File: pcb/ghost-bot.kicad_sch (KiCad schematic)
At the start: 42 parts, among them J1 Conn_01x03_Pin, J2 Conn_01x03_Pin, J3 Conn_01x04_Pin, J4 Conn_01x02_Pin, J5 Conn_01x05_Pin, J6 Conn_01x04_Pin, SW1 SW_Push, SW2 SW_Push, SW3 Switch

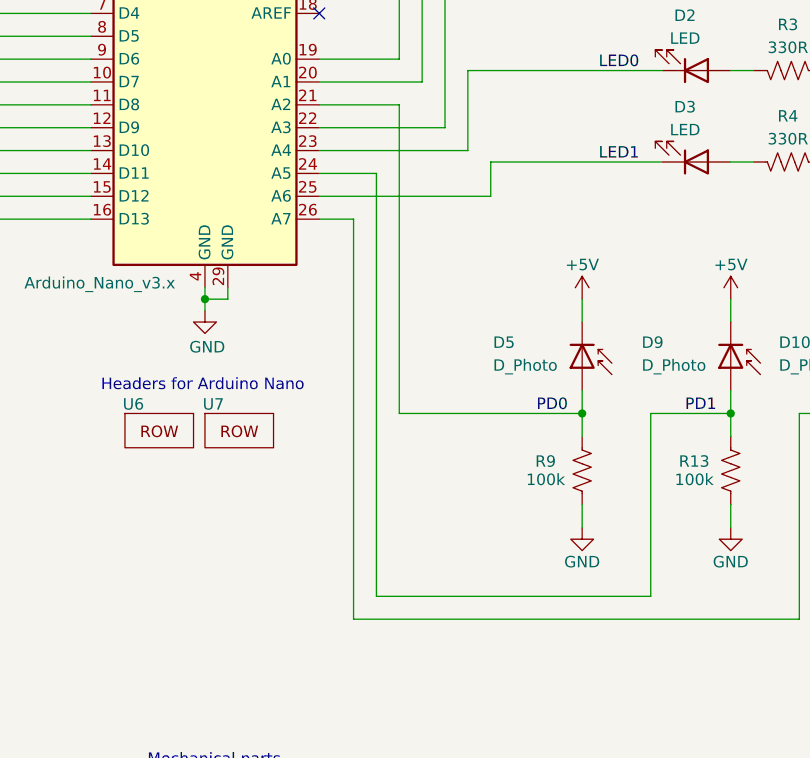
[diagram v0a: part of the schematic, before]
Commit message: Issue: Fix LED1 pin:  Attempted to swap A5 and A6 in schematic and PCB (although not sure what I may of broken in the mean time).
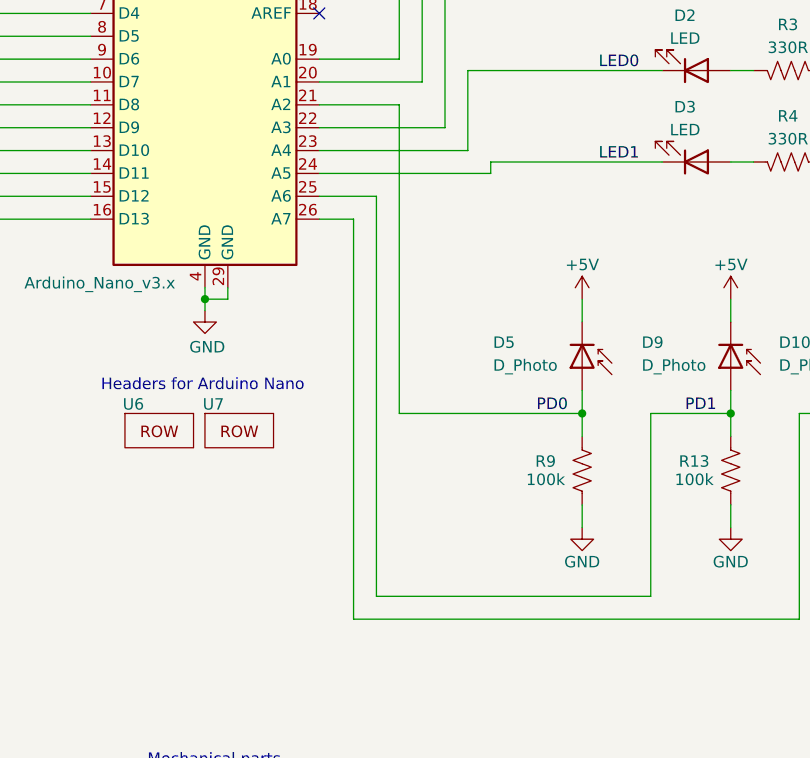
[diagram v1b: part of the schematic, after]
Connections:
- net LED1: now also A1.24 (A5); no longer A1.25 (A6)
- net PD1: now also A1.25 (A6); no longer A1.24 (A5)
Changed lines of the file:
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@@
+	(wire
+		(pts
+			(xy 165.1 99.06) (xy 184.15 99.06)
+		)
+		(stroke
+			(width 0)
+			(type default)
+		)
+	)
 	(wire
 		(pts
@@
 	(wire
 		(pts
+			(xy 165.1 101.6) (xy 171.45 101.6)
+		)
+		(stroke
+			(width 0)
+			(type default)
+		)
+	)
+	(wire
+		(pts
 			(xy 179.07 77.47) (xy 179.07 93.98)
 		)
@@
 	(wire
 		(pts
-			(xy 165.1 99.06) (xy 171.45 99.06)
-		)
-		(stroke
-			(width 0)
-			(type default)
-		)
-	)
-	(wire
-		(pts
 			(xy 238.76 115.57) (xy 241.3 115.57)
 		)
@@
 	(wire
 		(pts
-			(xy 165.1 101.6) (xy 184.15 101.6)
-		)
-		(stroke
-			(width 0)
-			(type default)
-		)
-	)
-	(wire
-		(pts
 			(xy 142.24 35.56) (xy 142.24 36.83)
 		)
@@
 	(wire
 		(pts
-			(xy 184.15 101.6) (xy 184.15 97.79)
+			(xy 184.15 99.06) (xy 184.15 97.79)
 		)
 		(stroke
@@
 	(wire
 		(pts
-			(xy 171.45 99.06) (xy 171.45 146.05)
-		)
-		(stroke
+			(xy 171.45 101.6) (xy 171.45 146.05)
+		)
+		(stroke
